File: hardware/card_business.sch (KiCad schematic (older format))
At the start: 11 parts, among them J1 Conn_01x01_Female, J2 USB_A, SW1 Reset, SW2 Boot, U1 CH552G

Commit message: change routing
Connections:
- net PAD: now also U1.2 (P1.4/T2/CAP1/SCS/TIN2/UCC1/AIN1); no longer U1.9 (P1.1/T2EX/CAP2/TIN1/VBUS2/AIN0)
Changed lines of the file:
@@
 Wire Notes Line
 	3150 1950 450  1950
-Text Label 3000 3550 2    50   ~ 0
+Text Label 3050 3550 2    50   ~ 0
 RST
 Wire Wire Line
-	3000 3550 3450 3550
+	3050 3550 3450 3550
 Text Label 6450 3250 0    50   ~ 0
 UDM
@@
 Wire Wire Line
 	10150 1100 10150 1150
-NoConn ~ 3450 2950
-Text Label 6550 3850 0    50   ~ 0
+NoConn ~ 6200 3850
+Text Label 3150 2950 2    50   ~ 0
 PAD
 Wire Wire Line
-	6550 3850 6200 3850
+	3150 2950 3450 2950
 $EndSCHEMATC

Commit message: Change pin name and routing update
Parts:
- SW1, SW2: footprint Connectors:C455281 -> Button_Switch_SMD:SW_SPST_TL3342
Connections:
- net UDM renamed UD-
- net UDP renamed UD+
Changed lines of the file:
@@
 F 0 "SW1" H 1600 1215 50  0000 C CNN
 F 1 "Reset" H 1600 1306 50  0000 C CNN
-F 2 "Connectors:C455281" H 1600 1600 50  0001 C CNN
+F 2 "Button_Switch_SMD:SW_SPST_TL3342" H 1600 1600 50  0001 C CNN
 F 3 "~" H 1600 1600 50  0001 C CNN
 	1    1600 1400
@@
 F 0 "SW2" H 10300 4385 50  0000 C CNN
 F 1 "Boot" H 10300 4294 50  0000 C CNN
-F 2 "Connectors:C455281" H 10300 4300 50  0001 C CNN
+F 2 "Button_Switch_SMD:SW_SPST_TL3342" H 10300 4300 50  0001 C CNN
 F 3 "~" H 10300 4300 50  0001 C CNN
 	1    10300 4100
@@
 	10250 3150 10100 3150
 Text Label 9550 1450 0    50   ~ 0
-UDM
+UD-
 Wire Wire Line
 	9850 1450 9550 1450
 Text Label 9400 1550 2    50   ~ 0
-UDP
+UD+
 Text Notes 10850 900  2    98   ~ 0
 Conexión del disp USB\n
@@
 	3050 3550 3450 3550
 Text Label 6450 3250 0    50   ~ 0
-UDM
+UD-
 Text Label 6450 3400 0    50   ~ 0
-UDP
+UD+
 Text Label 6450 3700 0    50   ~ 0
 P3.3
@@
 	10100 4100 9850 4100
 Text Label 9500 4100 2    50   ~ 0
-UDP
+UD+
 Wire Wire Line
 	9500 4100 9650 4100

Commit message: update traces v1.0
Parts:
- J2: symbol Connector:USB_A -> card_business-rescue:USB_A-Connector
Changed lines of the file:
@@
 	9000 450  9000 4200
 $Comp
-L Connector:USB_A J2
+L card_business-rescue:USB_A-Connector J2
 U 1 1 600C62B1
 P 10150 1550

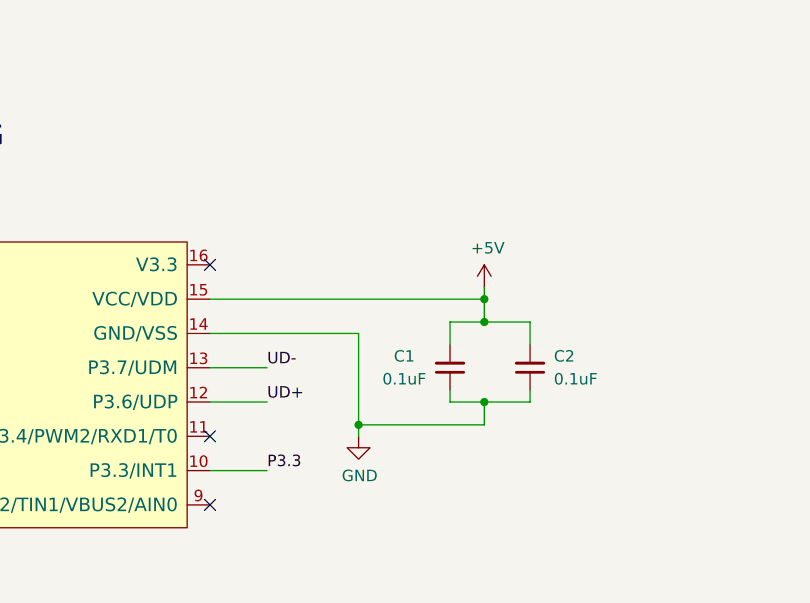
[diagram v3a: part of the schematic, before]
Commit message: add capacitor, modify traces
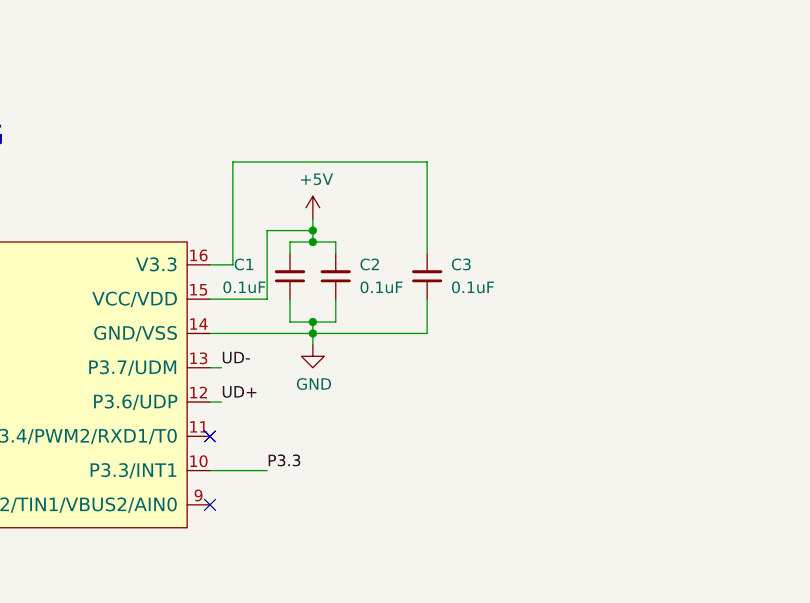
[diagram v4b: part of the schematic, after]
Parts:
- added C3: 0.1uF, Capacitor_SMD:C_0805_2012Metric, symbol Device:C_Small
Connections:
- net GND: now also C3.1
- net at U1.16 (V3.3): now also C3.2
- no-connect marks 10 -> 9
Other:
- moved on the sheet: C1, C2
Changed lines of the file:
@@
 L power:+5V #PWR03
 U 1 1 600F60B3
-P 7400 2900
-F 0 "#PWR03" H 7400 2750 50  0001 C CNN
-F 1 "+5V" H 7415 3073 50  0000 C CNN
-F 2 "" H 7400 2900 50  0001 C CNN
-F 3 "" H 7400 2900 50  0001 C CNN
-	1    7400 2900
+P 6650 2600
+F 0 "#PWR03" H 6650 2450 50  0001 C CNN
+F 1 "+5V" H 6665 2773 50  0000 C CNN
+F 2 "" H 6650 2600 50  0001 C CNN
+F 3 "" H 6650 2600 50  0001 C CNN
+	1    6650 2600
 	1    0    0    -1
 $EndComp
@@
 L Device:C_Small C2
 U 1 1 600F8100
-P 7600 3250
-F 0 "C2" H 7450 3200 50  0000 C CNN
-F 1 "0.1uF" H 7400 3300 50  0000 C CNN
-F 2 "Capacitor_SMD:C_0805_2012Metric" H 7600 3250 50  0001 C CNN
-F 3 "~" H 7600 3250 50  0001 C CNN
-	1    7600 3250
+P 6750 2850
+F 0 "C2" H 6600 2800 50  0000 C CNN
+F 1 "0.1uF" H 6550 2900 50  0000 C CNN
+F 2 "Capacitor_SMD:C_0805_2012Metric" H 6750 2850 50  0001 C CNN
+F 3 "~" H 6750 2850 50  0001 C CNN
+	1    6750 2850
 	-1   0    0    1
 $EndComp
@@
 L Device:C_Small C1
 U 1 1 600F88D9
-P 7250 3250
-F 0 "C1" H 7450 3200 50  0000 C CNN
-F 1 "0.1uF" H 7450 3300 50  0000 C CNN
-F 2 "Capacitor_SMD:C_0805_2012Metric" H 7250 3250 50  0001 C CNN
-F 3 "~" H 7250 3250 50  0001 C CNN
-	1    7250 3250
+P 6550 2850
+F 0 "C1" H 6750 2800 50  0000 C CNN
+F 1 "0.1uF" H 6750 2900 50  0000 C CNN
+F 2 "Capacitor_SMD:C_0805_2012Metric" H 6550 2850 50  0001 C CNN
+F 3 "~" H 6550 2850 50  0001 C CNN
+	1    6550 2850
 	-1   0    0    1
 $EndComp
@@
 Wire Wire Line
 	3050 3550 3450 3550
-Text Label 6450 3250 0    50   ~ 0
+Text Label 6250 3250 0    50   ~ 0
 UD-
-Text Label 6450 3400 0    50   ~ 0
+Text Label 6250 3400 0    50   ~ 0
 UD+
 Text Label 6450 3700 0    50   ~ 0
@@
 L power:GND #PWR02
 U 1 1 6015C8B7
-P 6850 3550
-F 0 "#PWR02" H 6850 3300 50  0001 C CNN
-F 1 "GND" H 6855 3377 50  0000 C CNN
-F 2 "" H 6850 3550 50  0001 C CNN
-F 3 "" H 6850 3550 50  0001 C CNN
-	1    6850 3550
-	1    0    0    -1
-$EndComp
-Wire Wire Line
-	6850 3100 6200 3100
-Wire Wire Line
-	6450 3250 6200 3250
-Wire Wire Line
-	6450 3400 6200 3400
+P 6650 3150
+F 0 "#PWR02" H 6650 2900 50  0001 C CNN
+F 1 "GND" H 6655 2977 50  0000 C CNN
+F 2 "" H 6650 3150 50  0001 C CNN
+F 3 "" H 6650 3150 50  0001 C CNN
+	1    6650 3150
+	1    0    0    -1
+$EndComp
+Wire Wire Line
+	6250 3250 6200 3250
+Wire Wire Line
+	6250 3400 6200 3400
 Wire Wire Line
 	6450 3700 6200 3700
 Wire Notes Line
 	3150 1950 3150 450
-Wire Wire Line
-	7600 3150 7600 3050
-Wire Wire Line
-	7250 3050 7250 3150
-Wire Wire Line
-	7600 3350 7600 3400
-Wire Wire Line
-	7250 3400 7250 3350
-Wire Wire Line
-	6850 3100 6850 3500
-Wire Wire Line
-	7250 3050 7400 3050
-Wire Wire Line
-	7250 3400 7400 3400
-Wire Wire Line
-	7400 2900 7400 2950
-Wire Wire Line
-	7400 2950 6200 2950
-Wire Wire Line
-	7400 2950 7400 3050
-Connection ~ 7400 2950
-Connection ~ 7400 3050
-Wire Wire Line
-	7400 3050 7600 3050
-Wire Wire Line
-	7400 3400 7400 3500
-Wire Wire Line
-	7400 3500 6850 3500
-Connection ~ 7400 3400
-Wire Wire Line
-	7400 3400 7600 3400
-Connection ~ 6850 3500
-Wire Wire Line
-	6850 3500 6850 3550
-NoConn ~ 6200 2800
 $Comp
 L Connector:Conn_01x01_Female J1
@@
 Wire Wire Line
 	3150 2950 3450 2950
+$Comp
+L Device:C_Small C3
+U 1 1 602D8C97
+P 7150 2850
+F 0 "C3" H 7000 2800 50  0000 C CNN
+F 1 "0.1uF" H 6950 2900 50  0000 C CNN
+F 2 "Capacitor_SMD:C_0805_2012Metric" H 7150 2850 50  0001 C CNN
+F 3 "~" H 7150 2850 50  0001 C CNN
+	1    7150 2850
+	-1   0    0    1
+$EndComp
+Wire Wire Line
+	6550 2950 6550 3050
+Wire Wire Line
+	6550 3050 6650 3050
+Wire Wire Line
+	6750 3050 6750 2950
+Connection ~ 6650 3050
+Wire Wire Line
+	6650 3050 6750 3050
+Wire Wire Line
+	6550 2750 6550 2700
+Wire Wire Line
+	6750 2700 6750 2750
+Wire Wire Line
+	6550 2700 6650 2700
+Connection ~ 6650 2700
+Wire Wire Line
+	6650 2700 6750 2700
+Wire Wire Line
+	6650 2600 6650 2650
+Wire Wire Line
+	6650 3050 6650 3100
+Wire Wire Line
+	6200 3100 6650 3100
+Connection ~ 6650 3100
+Wire Wire Line
+	6650 3100 6650 3150
+Wire Wire Line
+	6200 2950 6450 2950
+Wire Wire Line
+	6450 2950 6450 2650
+Wire Wire Line
+	6450 2650 6650 2650
+Connection ~ 6650 2650
+Wire Wire Line
+	6650 2650 6650 2700
+Wire Wire Line
+	7150 2950 7150 3100
+Wire Wire Line
+	7150 3100 6650 3100
+Wire Wire Line
+	6200 2800 6300 2800
+Wire Wire Line
+	6300 2800 6300 2350
+Wire Wire Line
+	6300 2350 7150 2350
+Wire Wire Line
+	7150 2350 7150 2750
 $EndSCHEMATC
